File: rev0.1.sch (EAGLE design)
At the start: 7 parts, among them U1 EFM32LG332F256G-E-QFP64, U2 FGPMMOPA6H, U3 NL-SW-LTE-GELS3-C

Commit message: made parts!
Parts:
- removed C1, C2, C3: .1uF, resistor:C-USC0603
- removed R1: (no value), resistor:R-US_R0603
- added C4: (no value), resistor:C-USC0402
- added IC1: MCP73811/2, adafruit:MCP73811/2
- added J2: (no value), SparkFun-Connectors:USB_MICRO-B_SMT
- added R2, R3: 4.7K, resistor:R-US_R0402
- added U4: TITAN-X1-GMS-3302, clackboard_lib:TITAN-X1-GMS-3302
- added U5: AT45DB161E-SHD2B-T, clackboard_lib:AT45DB161E-SHD2B-T
- added U6: LSM6DSL, clackboard_lib:LSM6DSL
- U1: value EFM32LG332F256G-E-QFP64 -> PIC24FJ128GB204; device clackboard_lib:EFM32LG332F256G-E-QFP64 -> clackboard_lib:PIC24FJ128GB204
- U2: value FGPMMOPA6H -> TELIT_RE866; device clackboard_lib:FGPMMOPA6H -> clackboard_lib:TELIT_RE866
- U3: value NL-SW-LTE-GELS3-C -> 24LC32A-SOT23-5; device clackboard_lib:NL-SW-LTE-GELS3-C -> clackboard_lib:24LC32A-SOT23-5
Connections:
- removed net +3V3: C1.1, C2.1, U2.VCC, U3.VCC
- new net 3.3V: C4.1, R2.2, R3.2, U3.VCC, U5.VCC
- new net CS: U5.CS
- new net MISO: U5.SO
- new net MOSI: U5.SI
- new net RESET: U5.RESET
- new net SCK: U5.SCK
- new net SCL: R2.1, U1.AN5/C1INA/RP3/SCL2/CTED8/CN7/PMWR/RB3, U3.SCL, U6.SCL
- new net SDA: R3.1, U1.AN4/C1INB/RP2/SDA2/T5CK/T4CK/CTED13/CN6/PMD2/RB2, U3.SDA, U6.SDA
- new net USB_N: J2.D-, U1.REFI/RP11/CTED9/CN15/PGC2/D-/RB11
- new net USB_P: J2.D+, U1.RP10/CTED11/CN16/PGD2/D+/RB10
- new net V_USB: J2.VBUS
- new net WP: U5.WP
- net GND: now also C4.2, J2.GND, J2.SHIELD, U1.AVSS/VSS@16, U1.VSS@29, U1.VSS@39, U2.GND@C3, U2.GND@D1, U2.GND@D2, U2.GND@E3, U2.GND@F1, U2.GND@F2, U2.GND@F3, U2.GND@F6, U2.GND@G1, U2.GND@G3, U3.VSS, U3.WP, U4.GND@1, U4.GND@10, U4.GND@11, U4.GND@24, U4.GND@3, U4.GND@4, U4.GND@5, U4.GND@6, U4.GND@9, U5.GND, U6.GND@6, U6.GND@7, U6.SDO/SA0; no longer C1.2, C2.2, U2.GND, U3.GND@10, U3.GND@11, U3.GND@15, U3.GND@4
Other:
- note added: "For the SOT-23 and chip scale packages, the address pins are not available. During device addressing, the A1, A2, and A0 Chip Selects bits should be set to ‘0’."
- note added: "I2C address: 1101010b"
- note added: "i2c"
- note added: "spi"
- note added: "spi/i2c"

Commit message: added bat management
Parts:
- added BAT+, BAT-: PTR1B2,54, testpad:PTR1B2,54
- added C1, C2, C3, C5, C6, C8: 0.1uF, resistor:C-USC0402
- added C10, C9: 22pF, resistor:C-USC0402
- added C11: 1uF, resistor:C-USC0603
- added C7: 10uF, resistor:C-USC0603
- added CON1: SIMCARD_HOLDER_693022010811, clackboard_lib:SIMCARD_HOLDER_693022010811
- added L1: MPZ1608D300BTA00, SparkFun-Coils:INDUCTOR-0402-3.9NH
- added R1, R5: 10K, resistor:R-US_R0402
- added R4: 100R, resistor:R-US_R0402
- added SJ1, SJ2: (no value), jumper:SJ
- added Y1: 16MHz, SparkFun-Clocks:CRYSTAL-16MHZSMD-5X3.2
- C4: value (none) -> 0.1uF
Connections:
- new net INT1: U6.INT1
- new net INT2: U6.INT2
- new net MCLR: R4.2, U1.MCLR
- new net N$1: SJ1.2, U6.SDX
- new net N$2: SJ2.2, U6.SCX
- new net N$3: R1.1, U6.CS
- new net N$5: C1.1, L1.1, U6.VDD
- new net N$6: C8.1, R4.1, R5.1
- new net N$7: C9.1, U1.OSCI/C1IND/CLKI/PMCS1/CN30/RA2, Y1.2
- new net N$8: C10.1, U1.OSCO/C2IND/CLKO/CN29/RA3, Y1.1
- new net N$9: C7.1, U1.VCAP
- new net RX0: U4.RX0
- new net TX0: U4.TX0
- new net VBAT: BAT+.TP, IC1.VBAT
- net 3.3V: now also C2.1, C3.1, C5.1, C6.1, L1.2, R1.2, R5.2, U1.AVDD@17, U1.VDD@28, U1.VDD@40, U1.VUSB_3V3, U6.VDDIO
- net GND: now also BAT-.TP, C1.2, C10.2, C11.2, C2.2, C3.2, C5.2, C6.2, C7.2, C8.2, C9.2, CON1.PAD1, CON1.PAD2, IC1.VSS, SJ1.1, SJ2.1
- net V_USB: now also C11.1, IC1.CE, IC1.PROG, IC1.VDD
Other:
- note added: "0x6A"
- note added: "GND"
- note added: "SIMCLK"
- note added: "SIMIO"
- note added: "SIMRST"
- note added: "SIMVCC"
- note added: "figure out where the sim data lines go"
- moved on the sheet: C4, IC1, R2, R3, U1, U2, U3, U4, U5, U6

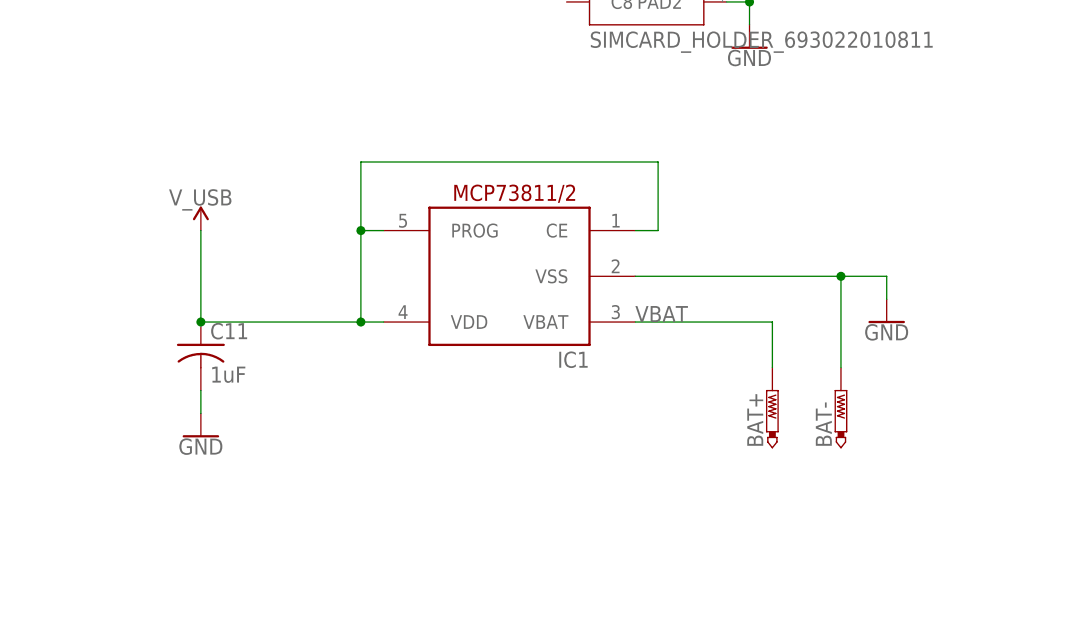
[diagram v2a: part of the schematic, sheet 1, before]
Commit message: reroute with new component placements
had a redo on the component placement for better routability, changed the battery charging circuit, still need to confirm which pins for communications go to the PIC. need to still add button.
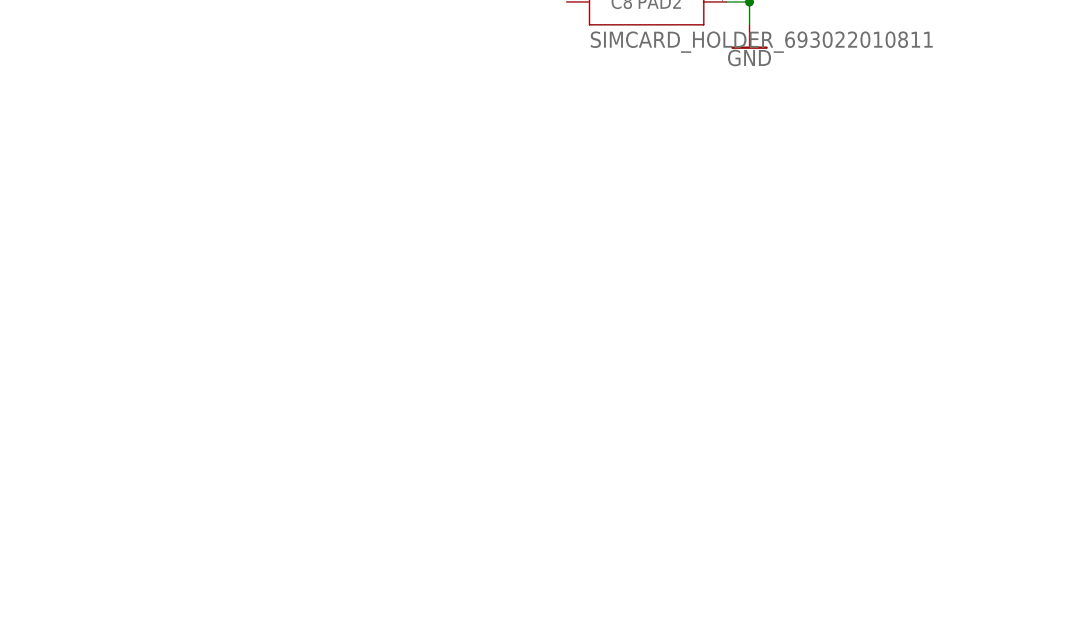
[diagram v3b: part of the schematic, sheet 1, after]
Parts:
- removed C11: 1uF, resistor:C-USC0603
- removed IC1: MCP73811/2, adafruit:MCP73811/2
- added C12: 10uF, resistor:C-USC0603
- added F1: 15K, adafruit:PTCFUSE-1206
- added IC2: MCP73871, adafruit:MCP73871
- added LED1: GREEN, adafruit:LEDCHIP-LED0603
- added LED2: ORANGE, adafruit:LEDCHIP-LED0603
- added R10, R7: 100K, resistor:R-US_R0402
- added R11, R8, R9: 1K, resistor:R-US_R0402
- added R6: 270K, resistor:R-US_R0402
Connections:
- new net 5V: IC2.OUT1, IC2.OUT2
- new net N$10: IC2.VPCC, R6.1, R7.2
- new net N$13: LED1.C, R8.2
- new net N$14: LED2.C, R9.2
- new net N$15: IC2.STAT2, R8.1
- new net N$16: IC2.STAT1/LBO, R9.1
- new net N$19: IC2.PROG3, R10.2
- new net N$20: IC2.PROG1, R11.2
- new net N$24: F1.1, IC2.THERM
- net GND: now also C12.2, F1.2, IC2.GND1, IC2.GND2, R10.1, R11.1, R7.1; no longer C11.2, IC1.VSS
- net VBAT: now also C12.1, IC2.VBAT1, IC2.VBAT2, IC2.VBAT3; no longer IC1.VBAT
- net V_USB: now also IC2./TE, IC2.CE, IC2.IN1, IC2.IN2, IC2.PROG2, IC2.SEL, LED1.A, LED2.A, R6.2; no longer C11.1, IC1.CE, IC1.PROG, IC1.VDD
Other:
- note added: "NTC"
- note added: "THERMISTOR"

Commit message: routed for PIC for cleaner routing
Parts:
- removed CON1: SIMCARD_HOLDER_693022010811, clackboard_lib:SIMCARD_HOLDER_693022010811
- added C11, C13: 10uF, resistor:C-USC0805
- added L2: 4.7µH/±30%/1.2A, SparkFun-Coils:INDUCTOR-CDRH-4.7UH
- added R12: 10K, resistor:R-US_R0402
- added SJ3: (no value), jumper:SJ
- added SW1: BUTTON-TL3330AF130QG, clackboard_lib:BUTTON-TL3330AF130QG
- added U7: PAM2305AAB330, clackboard_lib:PAM2305AAB330
- U6: SPICEPREFIX (none) -> X
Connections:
- new net BOOT0: U1.AN9/C3INA/RP15/T3CK/T2CK/CTED6/PMA14/CS1/CN11/PMCS/PMCS1/RB15, U2.BOOT0
- new net BUTTON: R12.1, SW1.1, U1.RP8/SCL1/CTED10/PMD4/CN22/USBOEN/RB8
- new net IUR_IN: U1.RP23/PMA0/PMALL/CN17/RC7, U2.IUR-IN#
- new net IUR_OUT: U1.AN7/C1INC/REFO/RP13/CTPLS/PMRD/CN13/RB13, U2.IUR-OUT#
- new net N$11: U4.VCC@7
- new net N$12: U2.VDD_NRF_LORA@E1, U2.VDD_NRF_LORA@E2
- new net N$17: L2.1, U7.SW
- new net N$18: SJ3.1, U2.RESET
- new net PGC: U1.AN3/C2INA/RP1/CTED12/CN5/PMD1/PGC1/RB1
- new net PGD: U1.AN2/CTCMP/C2INB/RP0/CN4/PGD1/HLVDIN/PMD0/RB0
- new net PIC_CTS: U1.RP22/PMA1/PMALH/CN18/RC6, U2.UART-RTS#
- new net PIC_RTS: U1.C1INC/C2INC/C3INC/RP9/SDA1/T1CK/CTED4/PMD3/CN21/RB9, U2.UART-CTS#
- new net PIC_RX: U1.RP24/PMA5/CN20/RC8, U2.UART-TXD
- new net PIC_TX: U1.RP25/CTED7/PMA6/CN19/RC9, U2.UART-RXD
- new net TELIT_RESET: SJ3.2, U1.RP7/CTED3/INT0/CN23/PMD5/RB7
- new net TESTMODE: U1.CVREF/AN6/C3INB/RP14/RTCC/CTED5/CN12/RB14, U2.TESTMODE
- net 3.3V: now also C13.1, L2.2, R12.2, U7.VOUT/FB
- net 5V: now also C11.1, U7.EN, U7.VIN
- net CS: now also U1.CN27/USBID/RB5
- net GND: now also C11.2, C13.2, SW1.2, SW1.MNT@1, SW1.MNT@2, U7.GND; no longer CON1.PAD1, CON1.PAD2
- net MISO: now also U1.SOSCI/CN1/RPI4/RB4
- net MOSI: now also U1.RP19/PMBE0/CN28/RC3
- net RESET: now also U1.AN11/RP17/CN9/RC1
- net RX0: now also U1.RP21/PMA3/CN26/RC5
- net SCK: now also U1.AN12/RP18/PMACK1/CN10/RC2
- net TX0: now also U1.RP20/PMA4/CN25/RC4
- net WP: now also U1.PMD6/CN24/VBUS/RB6
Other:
- note added: "MCU"
- note added: "POWER MANAGMENT"
- note added: "UART"
- note removed: "GND"
- note removed: "SIMCLK"
- note removed: "SIMIO"
- note removed: "SIMRST"
- note removed: "SIMVCC"
- note removed: "figure out where the sim data lines go"
- moved on the sheet: BAT+, BAT-, C1, C10, C12, C2, C3, C4, C5, C6, C7, C8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
